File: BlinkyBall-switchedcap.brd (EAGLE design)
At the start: 18 x 18 mm, 18 parts, among them U1 Tiny85-20-SMT

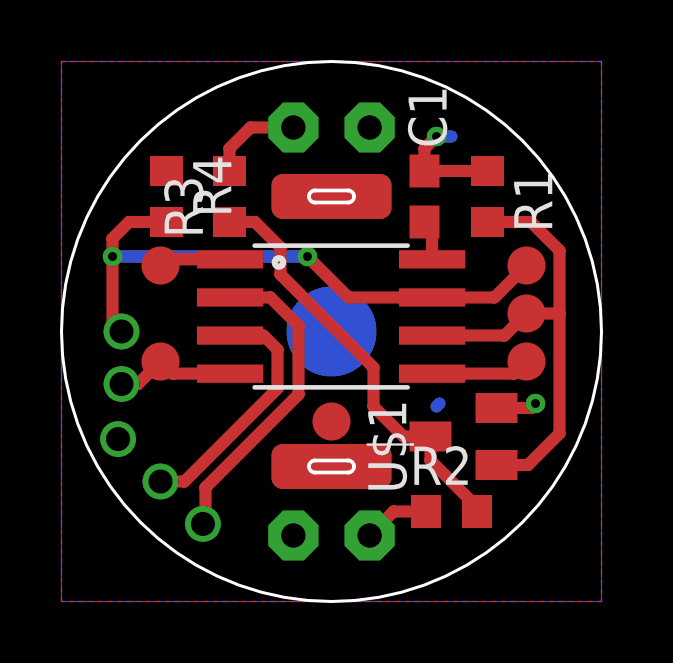
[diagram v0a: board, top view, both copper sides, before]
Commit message: Add switched-cap design for potential power boost
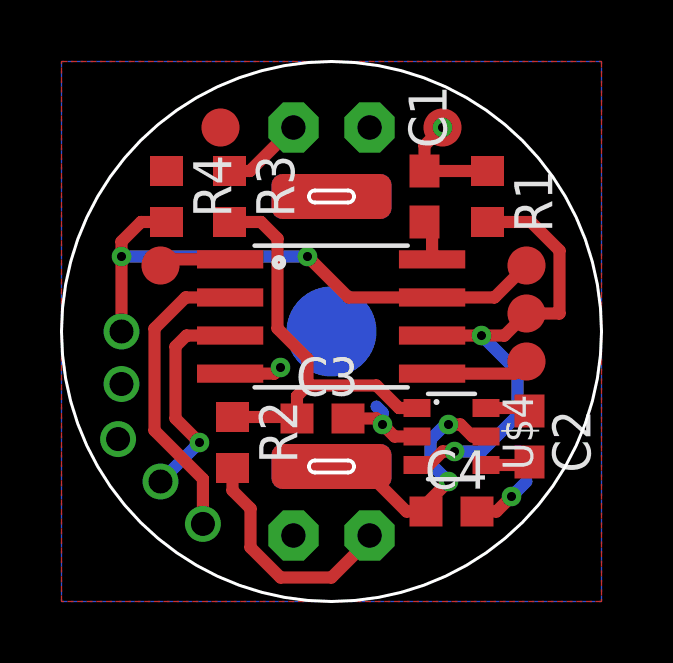
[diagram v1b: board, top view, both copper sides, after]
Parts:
- removed U$1: AO3418, blinkinlabs:SOT23
- added C2, C3, C4: 100nF, adafruit:C0603
- added U$4: REG71050, blinkinlabs:SOT23-6
- moved TP5 12.2 mm to (12.7, 15.8)
- moved TP4 10.5 mm to (5.30, 15.8)
- moved R2 7.65 mm to (5.70, 5.30), turned to 90 degrees
- turned LED_BOT to 0 degrees
- turned LED_TOP to 180 degrees
- turned R3 to 270 degrees
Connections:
- removed net N$3: LED_TOP.K, R3.2
- removed net N$4: R2.1, R3.1, U$1.3
- new net N$1: LED_TOP.A, R3.1
- new net N$6: C2.1, U$4.6
- new net N$7: C2.2, U$4.4
- new net N$9: C3.1, R2.2, R3.2, U$4.1
- net GND: now also C3.2, C4.2, LED_BOT.K, LED_TOP.K, U$4.2; no longer U$1.2
- net LED_TOP: now also U$4.3; no longer U$1.1
- net N$2: now also LED_BOT.A, R2.1; no longer LED_BOT.K, R2.2
- net V_BATT: now also C4.1, U$4.5; no longer LED_BOT.A, LED_TOP.A
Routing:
- net N$9: track 0.00 -> 14.5 mm
- net N$4: track 14.1 -> 0.00 mm
- net V_BATT: track 1.35 -> 10.3 mm, vias 0 -> 2
- net N$2: track 2.21 -> 7.94 mm
- net N$3: track 3.17 -> 0.00 mm
- net N$1: track 0.00 -> 2.73 mm
- net N$7: track 0.00 -> 1.49 mm
- net N$6: track 0.00 -> 1.49 mm
- net GND: track 9.52 -> 10.9 mm, vias 2 -> 4
- net IR_ENABLE: track 8.25 -> 7.34 mm, vias 0 -> 1
- net WAKEUP: track 20.1 -> 19.3 mm
- net LED_TOP: track 16.0 -> 16.6 mm, vias 0 -> 2
